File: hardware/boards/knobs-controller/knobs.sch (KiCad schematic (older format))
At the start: 0 parts

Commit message: redo migrate from eagle
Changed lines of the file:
@@
 EESchema Schematic File Version 4
+LIBS:knobs-cache
 EELAYER 30 0
 EELAYER END
 $Descr A4 11693 8268
 encoding utf-8
-Sheet 1 3
+Sheet 1 6
 Title ""
 Date ""
@@
 $Sheet
 S 1000 1000 500  150
-U 5D74D501
-F0 "KnobsController_1" 50
-F1 "KnobsController_1.sch" 50
+U 5D86641C
+F0 "knobs_1" 50
+F1 "knobs_1.sch" 50
 $EndSheet
 $Sheet
-S 1050 1500 500  150
-U 5D74D87C
-F0 "KnobsController_2" 50
-F1 "KnobsController_2.sch" 50
+S 3000 1000 500  150
+U 5D866797
+F0 "knobs_2" 50
+F1 "knobs_2.sch" 50
 $EndSheet
 $EndSCHEMATC

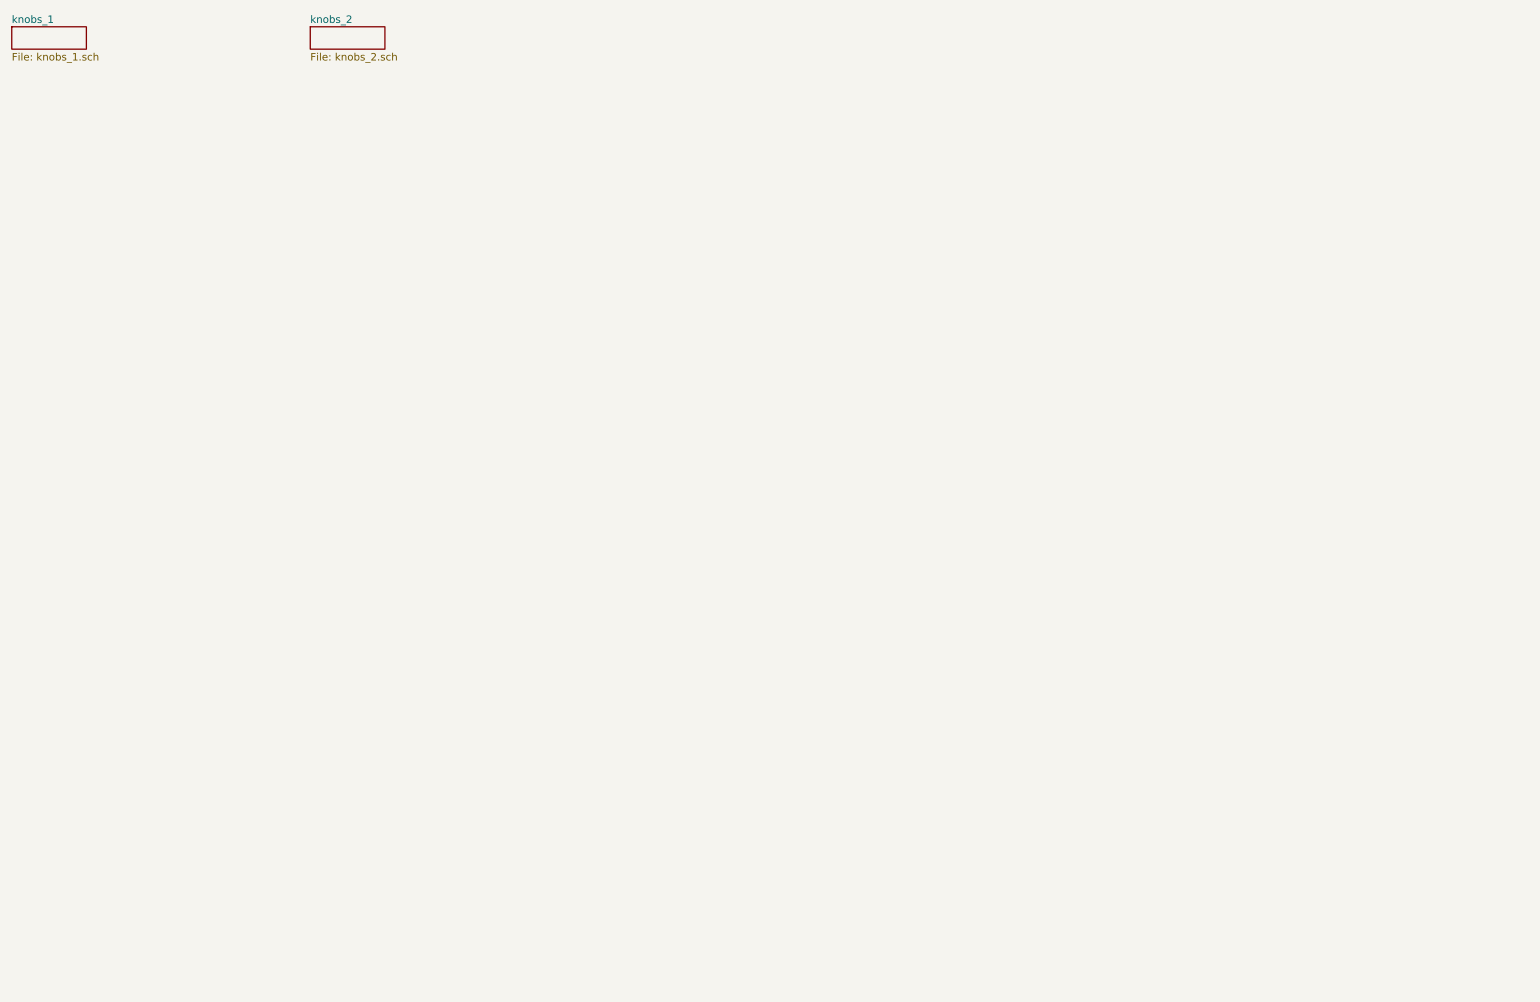
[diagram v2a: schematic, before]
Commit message: v1.7: merge knobs and top breakout in to single board, remove fpc connector, replace with standard 0.1' pin header
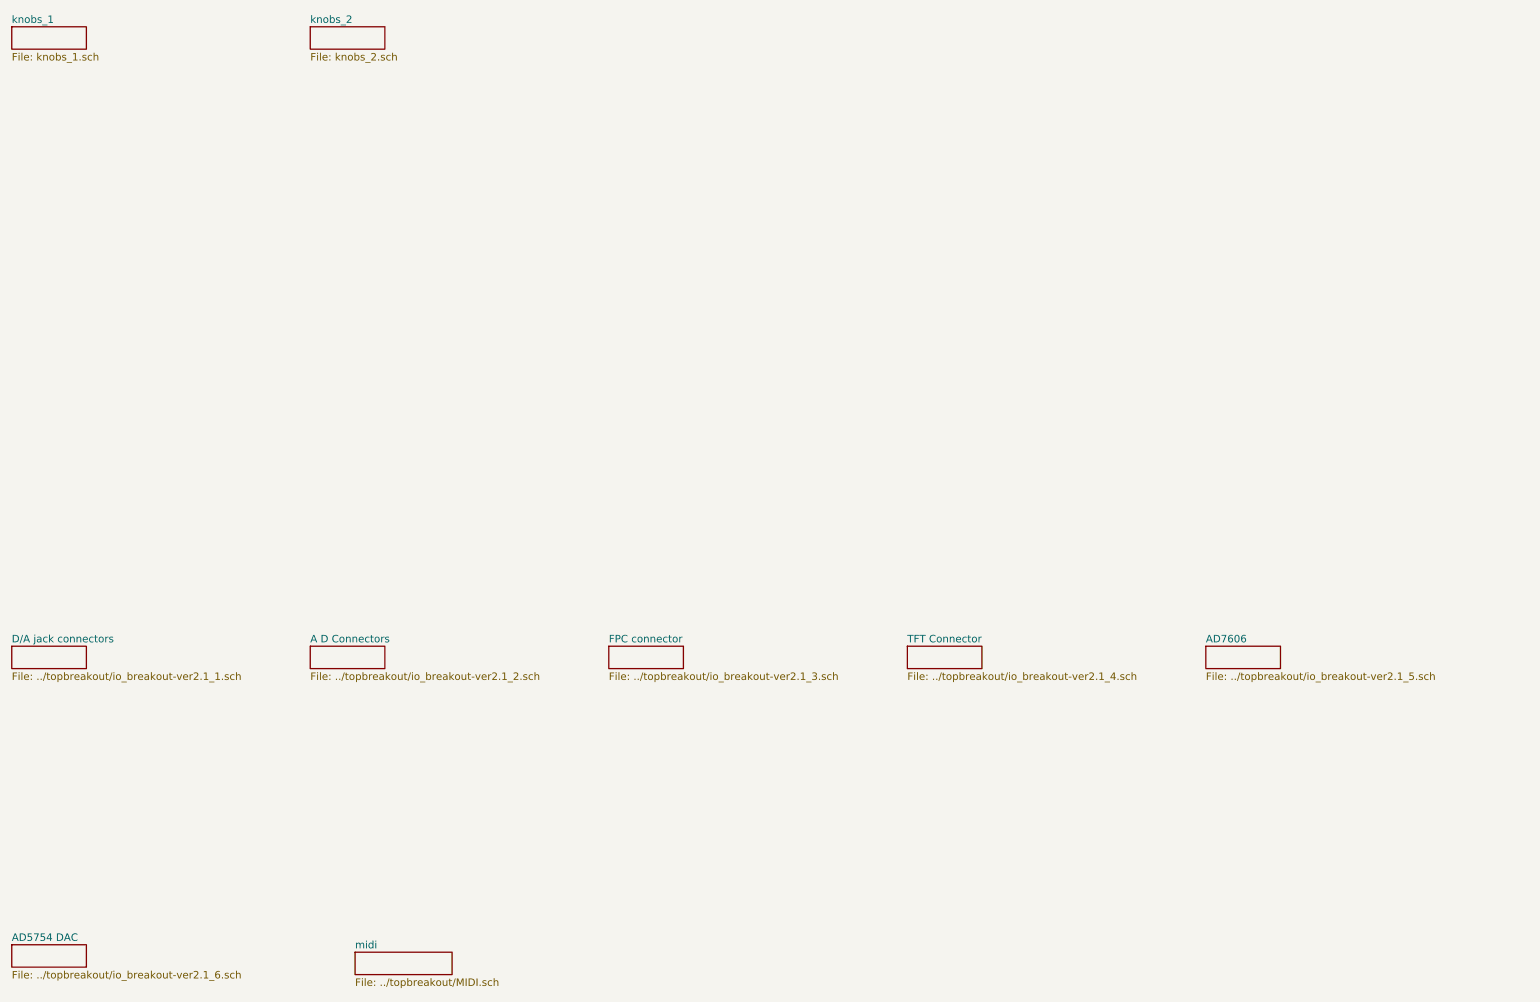
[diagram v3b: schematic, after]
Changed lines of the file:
@@
-EESchema Schematic File Version 5
+EESchema Schematic File Version 4
 EELAYER 30 0
 EELAYER END
 $Descr A4 11693 8268
 encoding utf-8
-Sheet 1 6
+Sheet 1 13
 Title ""
 Date ""
@@
 Comment3 ""
 Comment4 ""
-Comment5 ""
-Comment6 ""
-Comment7 ""
-Comment8 ""
-Comment9 ""
 $EndDescr
 $Sheet
@@
 F1 "knobs_2.sch" 50
 $EndSheet
+$Sheet
+S 1000 5150 500  150
+U 5D7F4208
+F0 "D/A jack connectors" 50
+F1 "../topbreakout/io_breakout-ver2.1_1.sch" 50
+$EndSheet
+$Sheet
+S 3000 5150 500  150
+U 5D7F4281
+F0 "A D Connectors" 50
+F1 "../topbreakout/io_breakout-ver2.1_2.sch" 50
+$EndSheet
+$Sheet
+S 5000 5150 500  150
+U 5D7F42FA
+F0 "FPC connector" 50
+F1 "../topbreakout/io_breakout-ver2.1_3.sch" 50
+$EndSheet
+$Sheet
+S 7000 5150 500  150
+U 5D7F4364
+F0 "TFT Connector" 50
+F1 "../topbreakout/io_breakout-ver2.1_4.sch" 50
+$EndSheet
+$Sheet
+S 9000 5150 500  150
+U 5D7F4383
+F0 "AD7606" 50
+F1 "../topbreakout/io_breakout-ver2.1_5.sch" 50
+$EndSheet
+$Sheet
+S 1000 7150 500  150
+U 5D7F4465
+F0 "AD5754 DAC" 50
+F1 "../topbreakout/io_breakout-ver2.1_6.sch" 50
+$EndSheet
+$Sheet
+S 3300 7200 650  150
+U 5D8CF794
+F0 "midi" 50
+F1 "../topbreakout/MIDI.sch" 50
+$EndSheet
 $EndSCHEMATC
